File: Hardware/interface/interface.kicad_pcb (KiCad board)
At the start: 2 copper layers, 21 parts, among them J1 TFmini1, J2 TFmini2, J3 TFmini3, U3 TS5A3357, U4 TXB0102DCT, U5 TS5A3357, U6 ARDUINO_MICRO_SHIELD

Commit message: Almost finish PCB routing
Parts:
- removed the U3 at (109.1, 69.1)
- removed U5: TS5A3357, Package_SO:VSSOP-8_3.0x3.0mm_P0.65mm
- removed U6: ARDUINO_MICRO_SHIELD, arduino_micro_shield:ARDUINO_MICRO_SHIELD
- added U4: ARDUINO_MICRO_SHIELD, arduino_micro_shield:ARDUINO_MICRO_SHIELD, F.Cu at (99.1, 86.8)
- C1, C12, C7: value 100µF-16V -> 100nF; footprint Capacitor_SMD:CP_Elec_6.3x5.7 -> Capacitor_SMD:C_1206_3216Metric_Pad1.33x1.80mm_HandSolder
- C11, C4, C5: value 100nF -> 100µF-16V; footprint Capacitor_SMD:C_1206_3216Metric_Pad1.33x1.80mm_HandSolder -> Capacitor_SMD:CP_Elec_6.3x5.7
- U1, U2: value ~ -> TS5A3357
- moved C1 98.2 mm to (192.0, 62.4), turned to 90 degrees
- moved C4 83.6 mm to (185.5, 60.3), turned to 90 degrees
- moved J1 81.1 mm to (196.5, 61.9)
- moved J3 71.2 mm to (53.5, 61.9)
- moved C9 49.5 mm to (137.9, 63.5), turned to 180 degrees
- moved C3 44.6 mm to (57.5, 62.6), turned to 90 degrees
- moved U1 37.8 mm to (77.5, 80.7)
- moved C10 36.1 mm to (112.8, 63.5), turned to 180 degrees
- moved U2 32.3 mm to (77.7, 72.0)
- moved C6 31.3 mm to (64.0, 60.3), turned to 90 degrees
- moved C12 30.5 mm to (77.7, 76.5), turned to 180 degrees
- moved C11 27.3 mm to (77.7, 63.5), turned to 180 degrees
- moved U3 25.7 mm to (91.2, 76.5), turned to -90 degrees
- moved C2 20.1 mm to (122.1, 57.5), turned to 180 degrees
- moved C5 17.4 mm to (112.8, 55.5), turned to 180 degrees
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- renumbered U4 to U3
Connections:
- C1 pad 1: +3V3 -> +5V
- C11 pad 1: +5V -> +3V3
- C12 pad 1: +5V -> +3V3
- C2 pad 1: +3V3 -> +5V
- C3 pad 1: +3V3 -> +5V
- C9 pad 1: +5V -> +3V3
- U1 pad 1: (no net) -> /RX_TF1
- U1 pad 2: (no net) -> /RX_TF2
- U1 pad 3: (no net) -> /RX_TF3
- U1 pad 5: (no net) -> /CMD_2
- U1 pad 6: (no net) -> /CMD_1
- U1 pad 7: (no net) -> Net-(U1A-COM)
- U2 pad 1: (no net) -> /TX_TF1
- U2 pad 2: (no net) -> /TX_TF2
- U2 pad 3: (no net) -> /TX_TF3
- U2 pad 5: (no net) -> /CMD_2
- U2 pad 6: (no net) -> /CMD_1
- U2 pad 7: (no net) -> Net-(U2A-COM)
- U3 pad 4: Net-(U4-A2) -> Net-(U2A-COM)
- U3 pad 5: Net-(U3A-COM) -> Net-(U1A-COM)
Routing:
- net +5V: track 0.00 -> 221.7 mm, vias 0 -> 2
- net /RX_TF1: track 0.00 -> 140.6 mm, vias 0 -> 2
- net GND: track 0.00 -> 135.0 mm, vias 0 -> 126
- net /TX_TF1: track 0.00 -> 131.4 mm, vias 0 -> 3
- net +3V3: track 0.00 -> 116.2 mm, vias 0 -> 2
- net /RX_TF2: track 0.00 -> 82.0 mm, vias 0 -> 1
- net /TX_TF2: track 0.00 -> 73.5 mm, vias 0 -> 1
- net /CMD_1: track 0.00 -> 62.4 mm, vias 0 -> 2
- net /CMD_2: track 0.00 -> 58.3 mm, vias 0 -> 2
- net /RX_TF3: track 0.00 -> 32.6 mm, vias 0 -> 1
- net /TX: track 0.00 -> 24.6 mm
- net /TX_TF3: track 0.00 -> 23.2 mm
- net /RX: track 0.00 -> 20.2 mm
- net Net-(U2A-COM): track 0.00 -> 11.4 mm
- net Net-(U1A-COM): track 0.00 -> 11.2 mm
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- added copper zone on B.Cu, net GND
- added copper zone on F.Cu, net GND
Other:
- board outline added: 150 x 40 mm

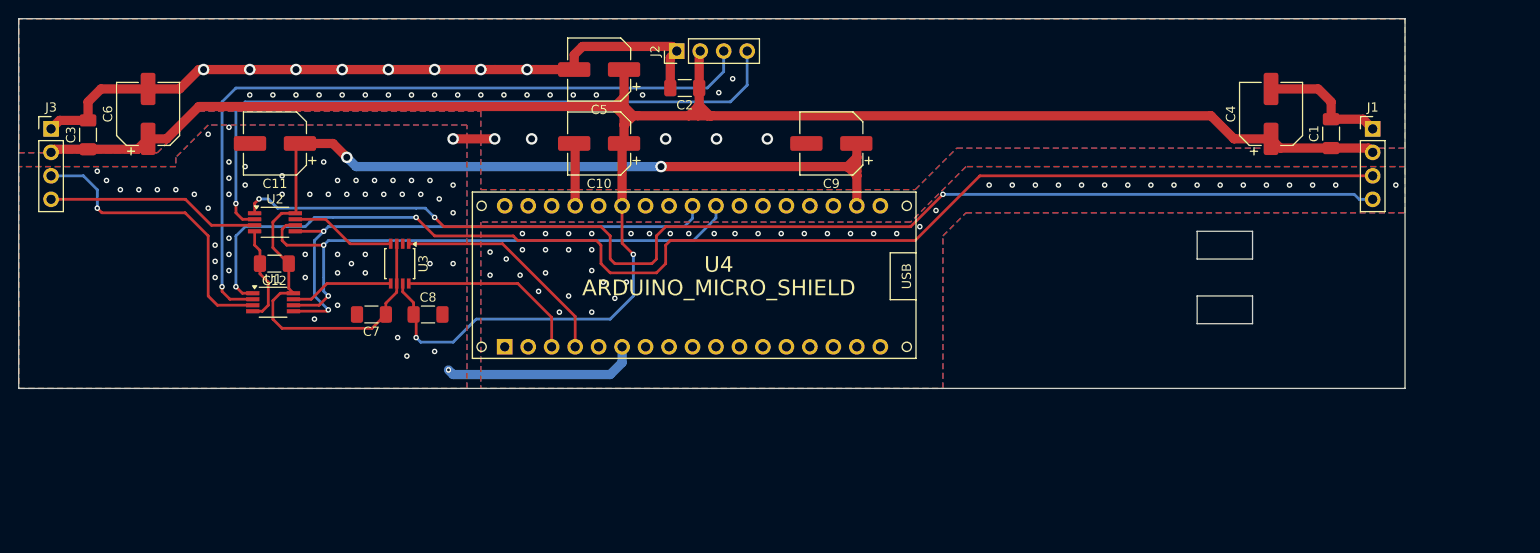
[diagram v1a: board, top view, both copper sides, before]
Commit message: PCB finished and update gitignore with kicad files
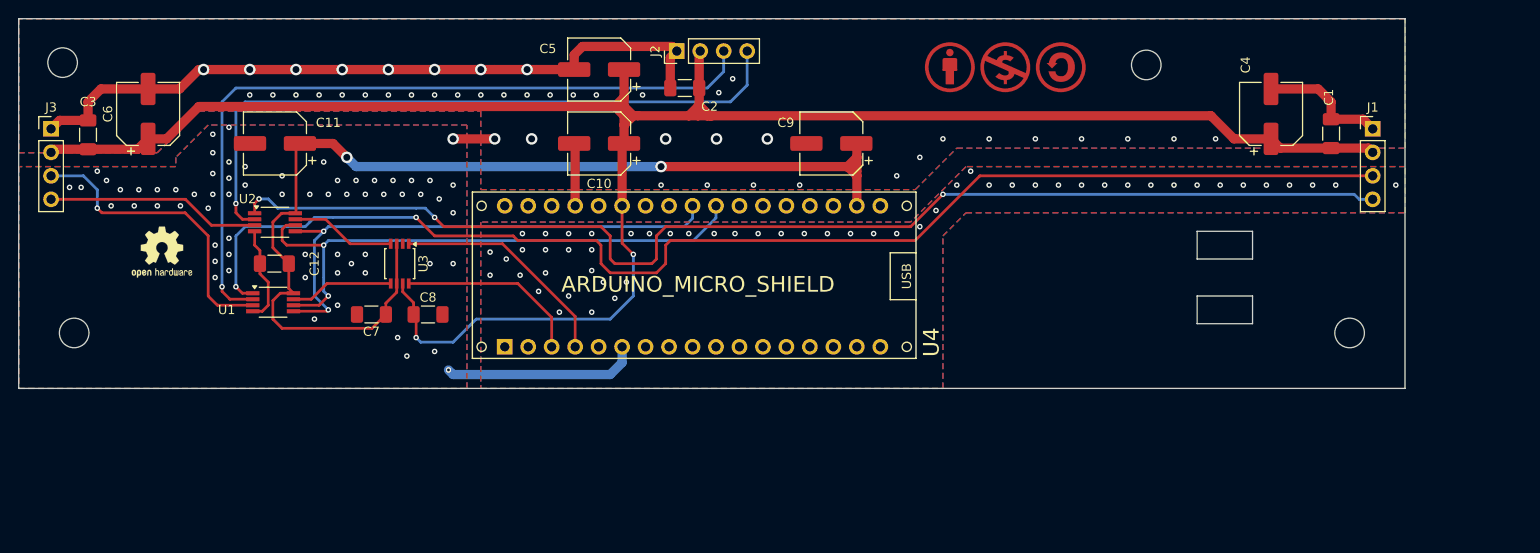
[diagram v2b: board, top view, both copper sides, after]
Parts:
- added REF**: Symbol_CC-Attribution_CopperTop_Small, Symbol:Symbol_CC-Attribution_CopperTop_Small, F.Cu at (150.8, 55.2)
- added REF**: MountingHole_3.2mm_M3, MountingHole:MountingHole_3.2mm_M3, F.Cu at (172.0, 55.0)
- added REF**: MountingHole_3.2mm_M3, MountingHole:MountingHole_3.2mm_M3, F.Cu at (194.0, 84.0)
- added REF**: MountingHole_3.2mm_M3, MountingHole:MountingHole_3.2mm_M3, F.Cu at (54.8, 54.8)
- added REF**: Symbol_CC-ShareAlike_CopperTop_Small, Symbol:Symbol_CC-ShareAlike_CopperTop_Small, F.Cu at (162.8, 55.2)
- added REF**: OSHW-Logo2_7.3x6mm_SilkScreen, Symbol:OSHW-Logo2_7.3x6mm_SilkScreen, F.Cu at (65.5, 75.2)
- added REF**: Symbol_CC-Noncommercial_CopperTop_Small, Symbol:Symbol_CC-Noncommercial_CopperTop_Small, F.Cu at (156.8, 55.2)
- added REF**: MountingHole_3.2mm_M3, MountingHole:MountingHole_3.2mm_M3, F.Cu at (56.0, 84.0)
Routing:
- net GND: vias 126 -> 150
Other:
- board text added: "Projet Antiphona - 2024 Alexandra Riss Concepteur: B. Bouchardon"

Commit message: Change sensor connectors to be more strong, efficient
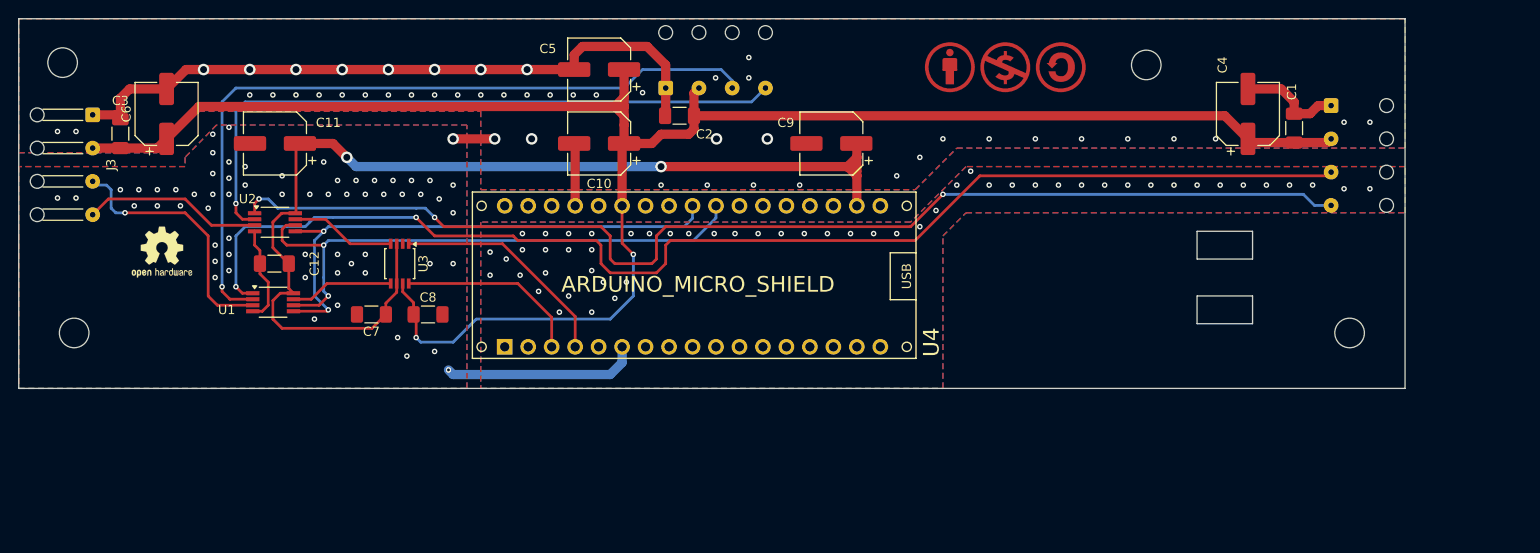
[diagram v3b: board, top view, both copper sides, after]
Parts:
- J1, J2: footprint Connector_PinHeader_2.54mm:PinHeader_1x04_P2.54mm_Vertical -> Connector_Wire:SolderWire-0.1sqmm_1x04_P3.6mm_D0.4mm_OD1mm_Relief; moved to B.Cu
- J3: footprint Connector_PinHeader_2.54mm:PinHeader_1x04_P2.54mm_Vertical -> Connector_Wire:SolderWire-0.1sqmm_1x04_P3.6mm_D0.4mm_OD1mm_Relief
- moved J1 5.16 mm to (192.0, 59.4), turned to -90 degrees
- moved J3 4.75 mm to (58.0, 60.4), turned to -90 degrees
- moved J2 4.18 mm to (120.0, 57.5), turned to 0 degrees
- moved C1 4.04 mm to (188.0, 61.8)
- moved C3 3.50 mm to (61.0, 62.4)
- moved C2 3.05 mm to (121.5, 60.5)
- moved C4 2.50 mm to (183.0, 60.3)
- moved C6 2.00 mm to (66.0, 60.3)
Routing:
- net +5V: track 221.7 -> 202.7 mm
- net GND: track 135.0 -> 128.4 mm, vias 150 -> 152
- net /RX_TF3: track 32.6 -> 27.9 mm
- net /RX_TF1: track 140.6 -> 136.3 mm
- net /TX_TF1: track 131.4 -> 127.2 mm
- net /TX_TF3: track 23.2 -> 19.4 mm
- net /TX_TF2: track 73.5 -> 71.6 mm
- net (no net): vias 15 -> 14
